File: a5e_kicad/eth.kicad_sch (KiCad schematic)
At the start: 52 parts, among them J9 RJ45_RB1-125B8G1A, U10 KSZ9031RNXCA, Y3 25MHz

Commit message: Add LCSC part numbers and fix C102 footprint
Add a hidden LCSC field to 290 symbols from the JLCPCB parts match
(2026-10-23). Left without LCSC: U7, U15, L1 (not in the JLCPCB
library), C1/C2/C4 and L2-L5 (no value specified), J3 (no confident
match) and Y3 (the 12 pF Basic crystal does not suit the 27 pF load
caps). U2, U12, Y2 and J9 carry the exact-MPN LCSC numbers although
they currently show zero JLCPCB stock.

C102 (22U 6V3) had a 0201 footprint; no 22 uF 0201 part exists. Change
it to 0402 (C415703) like C5-C7.
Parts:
- C18, C21, C24, C258, C27: LCSC (none) -> C415703
- C19, C20, C22, C23, C25, C255, C256, C257, C26, C28, C29, C30, C31, C32: LCSC (none) -> C1525
- C251, C252: LCSC (none) -> C1557
- C259: LCSC (none) -> C52923
- J9: LCSC (none) -> C363353
- R247: LCSC (none) -> C25744
- R250: LCSC (none) -> C25104
- R251, R252, R253, R254, R255, R256, R257, R258, R259, R260, R261, R262: LCSC (none) -> C25092
- R29, R30, R32, R34, R36, R37, R39, R40: LCSC (none) -> C25900
- R31, R33, R35, R38: LCSC (none) -> C11702
- R41: LCSC (none) -> C25852
- U10: LCSC (none) -> C58758

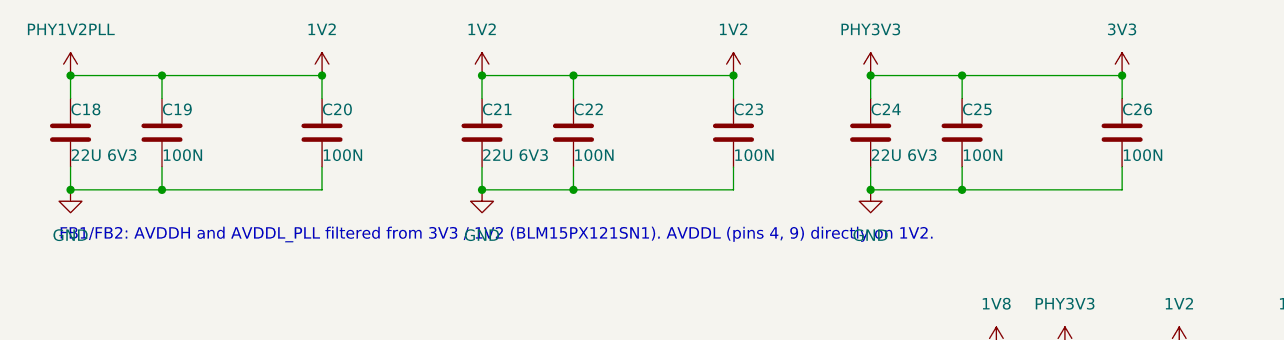
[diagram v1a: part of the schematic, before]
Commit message: Add PHY ferrite beads, restore LPDDR4 net classes, fix DRC rule loading
Ethernet PHY: FB1 (3V3 -> PHY3V3, AVDDH) and FB2 (1V2 -> PHY1V2PLL,
AVDDL_PLL), BLM15PX121SN1D 0402 (LCSC C88970). ETH_PHY_REVIEW.md and the
sheet note described them, but the parts were never added and the PHY
rail symbols sat on the same wire as 3V3/1V2.

Project: restore what ea166c5 dropped by mistake - the lpddr_ca and
lpddr_diff net classes, the dm/ca/diff netclass patterns, the lpddr_dq
width/tuning profile, both LPDDR4 tuning profiles (JLC08161H-3313
delays), the reserved designators, and the qspi_D[3..0] bus alias that
had been corrupted to qspi_D{3..0]. ea166c5's intended JLCPCB rule
changes are kept.

DRC rules: any condition using "NetClass matches" made KiCad 10.0.7
silently ignore the whole .kicad_dru, so none of the custom rules was
active. Nets also carry composite classes ("lpddr_ca,Default"), so
"NetClass == ..." never matched. Use hasNetclass() throughout.
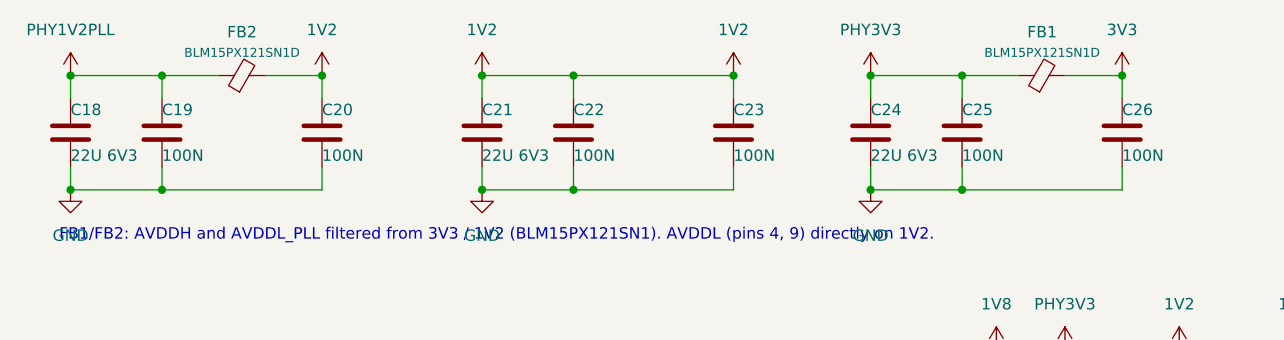
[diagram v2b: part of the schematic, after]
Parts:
- added FB1, FB2: BLM15PX121SN1D, Inductor_SMD:L_0402_1005Metric, symbol Device:FerriteBead_Small
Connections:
- net 1V2: now also FB2.2; no longer C18.1, C19.1, U10.44 (AVDDL_PLL)
- net 3V3: now also FB1.2; no longer C24.1, C25.1, U10.1 (AVDDH), U10.12 (AVDDH)
- new net PHY1V2PLL: C18.1, C19.1, FB2.1, U10.44 (AVDDL_PLL)
- new net PHY3V3: C24.1, C25.1, FB1.1, U10.1 (AVDDH), U10.12 (AVDDH)
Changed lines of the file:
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@@
 	(wire
 		(pts
-			(xy 135.89 22.86) (xy 153.67 22.86)
-		)
-		(stroke
-			(width 0)
-			(type default)
-		)
-	)
-	(wire
-		(pts
 			(xy 36.83 22.86) (xy 46.99 22.86)
 		)
@@
 	(wire
 		(pts
-			(xy 46.99 22.86) (xy 64.77 22.86)
-		)
-		(stroke
-			(width 0)
-			(type default)
-		)
-	)
-	(wire
-		(pts
 			(xy 172.72 55.88) (xy 172.72 53.34)
 		)
@@
 					(unit 1)
 				)
+			)
+		)
+	)
+	(wire
+		(pts
+			(xy 46.99 22.86) (xy 53.34 22.86)
+		)
+		(stroke
+			(width 0)
+			(type default)
+		)
+	)
+	(wire
+		(pts
+			(xy 58.42 22.86) (xy 64.77 22.86)
+		)
+		(stroke
+			(width 0)
+			(type default)
+		)
+	)
+	(wire
+		(pts
+			(xy 135.89 22.86) (xy 142.24 22.86)
+		)
+		(stroke
+			(width 0)
+			(type default)
+		)
+	)
+	(wire
+		(pts
+			(xy 147.32 22.86) (xy 153.67 22.86)
+		)
+		(stroke
+			(width 0)
+			(type default)
+		)
+	)
+	(symbol
+		(lib_id "Device:FerriteBead_Small")
+		(at 55.88 22.86 90)
+		(unit 1)
+		(body_style 1)
+		(exclude_from_sim no)
+		(in_bom yes)
+		(on_board yes)
+		(in_pos_files yes)
+		(dnp no)
+		(property "Reference" "FB2"
+			(at 55.88 18.03 90)
+			(show_name no)
+			(do_not_autoplace no)
+			(effects
+				(font
+					(size 1.27 1.27)
+				)
+			)
+		)
+		(property "Value" "BLM15PX121SN1D"
+			(at 55.88 20.32 90)
+			(show_name no)
+			(do_not_autoplace no)
+			(effects
+				(font
+					(size 1 1)
+				)
+			)
+		)
+		(property "Footprint" "Inductor_SMD:L_0402_1005Metric"
+			(at 55.88 22.86 0)
+			(hide yes)
+			(show_name no)
+			(do_not_autoplace no)
+			(effects
+				(font
+					(size 1.27 1.27)
+				)
+			)
+		)
+		(property "Datasheet" ""
+			(at 55.88 22.86 0)
+			(hide yes)
+			(show_name no)
+			(do_not_autoplace no)
+			(effects
+				(font
+					(size 1.27 1.27)
+				)
+			)
+		)
+		(property "Description" "Ferrite bead 120R@100MHz 1.5A 0402"
+			(at 55.88 22.86 0)
+			(hide yes)
+			(show_name no)
+			(do_not_autoplace no)
+			(effects
+				(font
+					(size 1.27 1.27)
+				)
+			)
+		)
+		(property "LCSC" "C88970"
+			(at 55.88 22.86 0)
+			(hide yes)
+			(show_name no)
+			(do_not_autoplace no)
+			(effects
+				(font
+					(size 1.27 1.27)
+				)
+			)
+		)
+		(pin "1"
+		)
+		(pin "2"
+		)
+		(instances
+			(project "agilex_3_soc"
+				(path "/a5b98d95-6877-4284-904f-d04e32723ae0/cf2987d8-8050-440f-9afe-54dd4a6786f5"
+					(reference "FB2")
+					(unit 1)
+				)
+			)
+		)
+	)
+	(symbol
+		(lib_id "Device:FerriteBead_Small")
+		(at 144.78 22.86 90)
+		(unit 1)
+		(body_style 1)
+		(exclude_from_sim no)
+		(in_bom yes)
+		(on_board yes)
+		(in_pos_files yes)
+		(dnp no)
+		(property "Reference" "FB1"
+			(at 144.78 18.03 90)
+			(show_name no)
+			(do_not_autoplace no)
+			(effects
+				(font
+					(size 1.27 1.27)
+				)
+			)
+		)
+		(property "Value" "BLM15PX121SN1D"
+			(at 144.78 20.32 90)
+			(show_name no)
+			(do_not_autoplace no)
+			(effects
+				(font
+					(size 1 1)
+				)
+			)
+		)
+		(property "Footprint" "Inductor_SMD:L_0402_1005Metric"
+			(at 144.78 22.86 0)
+			(hide yes)
+			(show_name no)
+			(do_not_autoplace no)
+			(effects
+				(font
+					(size 1.27 1.27)
+				)
+			)
+		)
+		(property "Datasheet" ""
+			(at 144.78 22.86 0)
+			(hide yes)
+			(show_name no)
+			(do_not_autoplace no)
+			(effects
+				(font
+					(size 1.27 1.27)
+				)
+			)
+		)
+		(property "Description" "Ferrite bead 120R@100MHz 1.5A 0402"
+			(at 144.78 22.86 0)
+			(hide yes)
+			(show_name no)
+			(do_not_autoplace no)
+			(effects
+				(font
+					(size 1.27 1.27)
+				)
+			)
+		)
+		(property "LCSC" "C88970"
+			(at 144.78 22.86 0)
+			(hide yes)
+			(show_name no)
+			(do_not_autoplace no)
+			(effects
+				(font
+					(size 1.27 1.27)
+				)
+			)
+		)
+		(pin "1"
+		)
+		(pin "2"
+		)
+		(instances
+			(project "agilex_3_soc"
+				(path "/a5b98d95-6877-4284-904f-d04e32723ae0/cf2987d8-8050-440f-9afe-54dd4a6786f5"
+					(reference "FB1")
+					(unit 1)
+				)

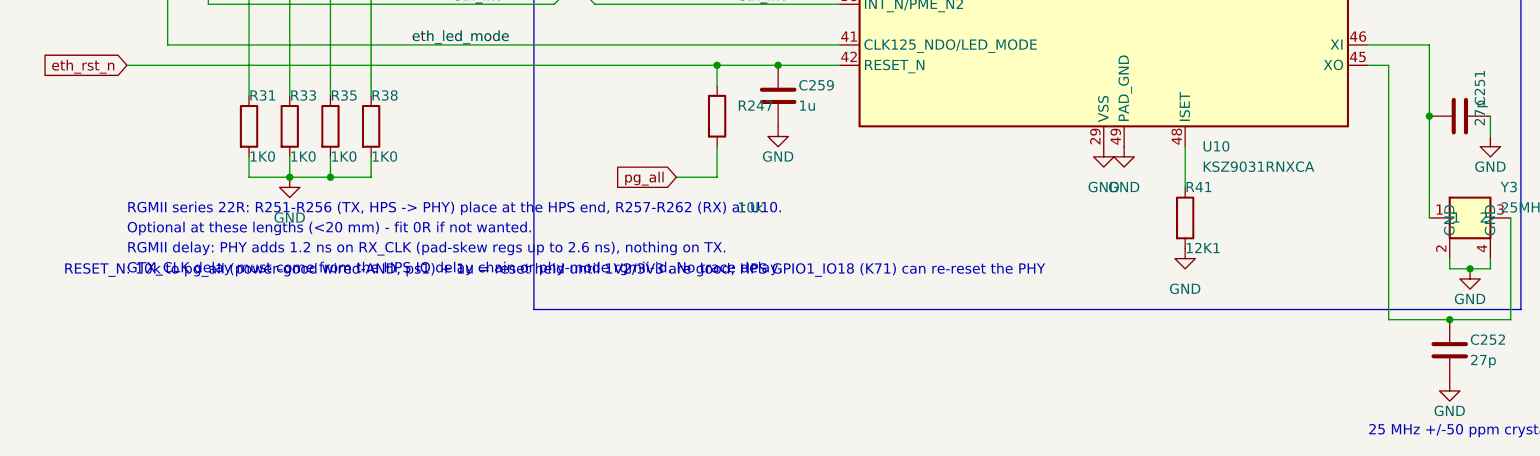
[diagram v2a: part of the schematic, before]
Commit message: PHY reset: pull RESET_N down instead of tying it to pg_all
R247 10k now goes to GND, so the KSZ9031 stays in reset until software
drives HPS GPIO1_IO18 (K71) high. The processor controls the reset, and
it is released only after all rails are up. Update the sheet note (and
move it off the RGMII notes) and ETH_PHY_REVIEW.md.
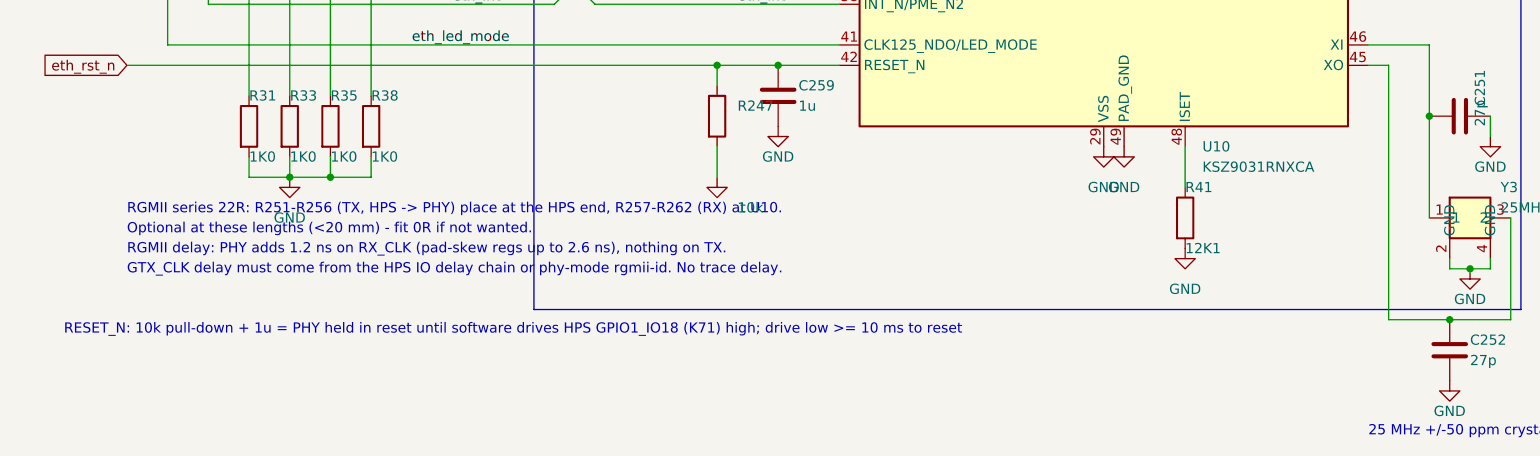
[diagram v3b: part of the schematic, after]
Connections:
- net pg_all is gone; now on net GND: R247.2
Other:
- note added: "RESET_N: 10k pull-down + 1u = PHY held in reset until software drives HPS GPIO1_IO18 (K71) high; drive low >= 10 ms to reset"
- note removed: "RESET_N: 10k to pg_all (power-good wired-AND, ps1) + 1u = reset held until 1V2/3V3 are good; HPS GPIO1_IO18 (K71) can re-reset the PHY"
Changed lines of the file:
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@@
 		)
 	)
-	(text "RESET_N: 10k to pg_all (power-good wired-AND, ps1) + 1u = reset held until 1V2/3V3 are good; HPS GPIO1_IO18 (K71) can re-reset the PHY"
+	(text "RESET_N: 10k pull-down + 1u = PHY held in reset until software drives HPS GPIO1_IO18 (K71) high; drive low >= 10 ms to reset"
 		(exclude_from_sim no)
-		(at 27.686 152.654 0)
+		(at 27.686 160.02 0)
 		(effects
 			(font
@@
 	(wire
 		(pts
-			(xy 109.22 140.97) (xy 104.14 140.97)
-		)
-		(stroke
-			(width 0)
-			(type default)
-		)
-	)
-	(wire
-		(pts
 			(xy 93.98 91.44) (xy 114.3 91.44)
 		)
@@
 		)
 	)
-	(global_label "pg_all"
-		(shape input)
-		(at 104.14 140.97 180)
-		(effects
-			(font
-				(size 1.27 1.27)
-			)
-			(justify right)
-		)
-		(property "Intersheetrefs" "${INTERSHEET_REFS}"
-			(at 104.14 140.97 0)
-			(hide yes)
-			(show_name no)
-			(do_not_autoplace no)
-			(effects
-				(font
-					(size 1.27 1.27)
-				)
-			)
-		)
-	)
 	(hierarchical_label "{hps_eth}"
 		(shape bidirectional)
@@
 					(unit 1)
 				)
+			)
+		)
+	)
+	(symbol
+		(lib_id "power:GND")
+		(at 109.22 140.97 0)
+		(unit 1)
+		(body_style 1)
+		(exclude_from_sim no)
+		(in_bom yes)
+		(on_board yes)
+		(in_pos_files yes)
+		(dnp no)
+		(property "Reference" "#PWR1551"
+			(at 109.22 147.32 0)
+			(hide yes)
+			(show_name no)
+			(do_not_autoplace no)
+			(effects
+				(font
+					(size 1.27 1.27)
+				)
+			)
+		)
+		(property "Value" "GND"
+			(at 109.22 144.78 0)
+			(hide yes)
+			(show_name no)
+			(do_not_autoplace no)
+			(effects
+				(font
+					(size 1.27 1.27)
+				)
+			)
+		)
+		(property "Footprint" ""
+			(at 109.22 140.97 0)
+			(hide yes)
+			(show_name no)
+			(do_not_autoplace no)
+			(effects
+				(font
+					(size 1.27 1.27)
+				)
+			)
+		)
+		(property "Datasheet" ""
+			(at 109.22 140.97 0)
+			(hide yes)
+			(show_name no)
+			(do_not_autoplace no)
+			(effects
+				(font
+					(size 1.27 1.27)
+				)
+			)
+		)
+		(property "Description" "Power symbol creates a global label with name \"GND\""
+			(at 109.22 140.97 0)
+			(hide yes)
+			(show_name no)
+			(do_not_autoplace no)
+			(effects
+				(font
+					(size 1.27 1.27)
+				)
+			)
+		)
+		(pin "1"
+		)
+		(instances
+			(project "agilex_3_soc"
+				(path "/a5b98d95-6877-4284-904f-d04e32723ae0/cf2987d8-8050-440f-9afe-54dd4a6786f5"
+					(reference "#PWR1551")
+					(unit 1)
+				)
